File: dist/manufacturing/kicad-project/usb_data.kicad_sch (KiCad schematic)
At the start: 8 parts, among them J10 J10

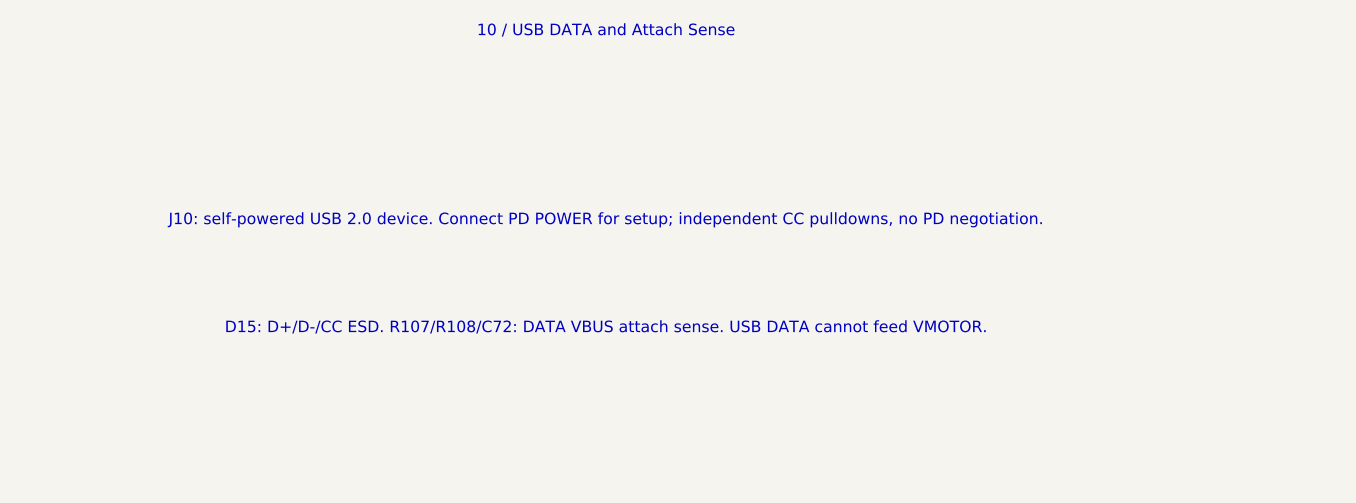
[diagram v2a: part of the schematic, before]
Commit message: Complete top-side routing and verify reference-board ECO
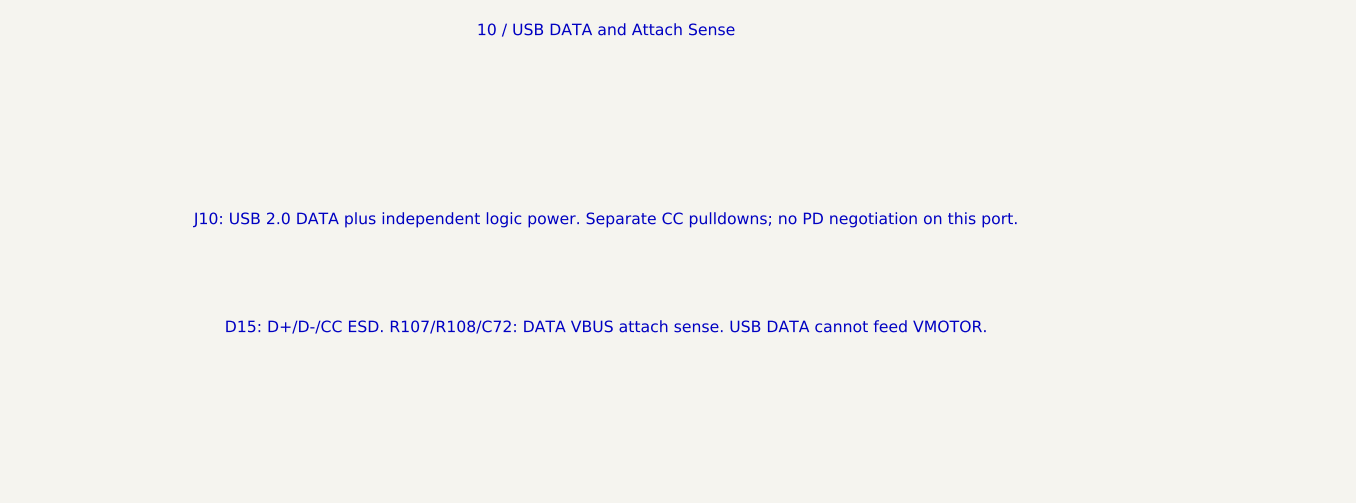
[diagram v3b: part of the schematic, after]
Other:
- note added: "J10: USB 2.0 DATA plus independent logic power. Separate CC pulldowns; no PD negotiation on this port."
- note removed: "J10: self-powered USB 2.0 device. Connect PD POWER for setup; independent CC pulldowns, no PD negotiation."
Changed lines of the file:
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@@
     (instances
       (project ""
-        (path "/4ef2daa1-40fc-426a-abb2-c834ba40a3c9/d0985985-ab5f-41ca-a28b-92bc3b6995fd"
+        (path "/953e0ace-4c89-4879-a4e2-9aa73ffc3208/12d136b2-94e5-4882-b24e-859549138c6a"
           (reference "R107")
           (unit 1)
@@
     (instances
       (project ""
-        (path "/4ef2daa1-40fc-426a-abb2-c834ba40a3c9/d0985985-ab5f-41ca-a28b-92bc3b6995fd"
+        (path "/953e0ace-4c89-4879-a4e2-9aa73ffc3208/12d136b2-94e5-4882-b24e-859549138c6a"
           (reference "R108")
           (unit 1)
@@
     (instances
       (project ""
-        (path "/4ef2daa1-40fc-426a-abb2-c834ba40a3c9/d0985985-ab5f-41ca-a28b-92bc3b6995fd"
+        (path "/953e0ace-4c89-4879-a4e2-9aa73ffc3208/12d136b2-94e5-4882-b24e-859549138c6a"
           (reference "C72")
           (unit 1)
@@
     (instances
       (project ""
-        (path "/4ef2daa1-40fc-426a-abb2-c834ba40a3c9/d0985985-ab5f-41ca-a28b-92bc3b6995fd"
+        (path "/953e0ace-4c89-4879-a4e2-9aa73ffc3208/12d136b2-94e5-4882-b24e-859549138c6a"
           (reference "J10")
           (unit 1)
@@
     (instances
       (project ""
-        (path "/4ef2daa1-40fc-426a-abb2-c834ba40a3c9/d0985985-ab5f-41ca-a28b-92bc3b6995fd"
+        (path "/953e0ace-4c89-4879-a4e2-9aa73ffc3208/12d136b2-94e5-4882-b24e-859549138c6a"
           (reference "R105")
           (unit 1)
@@
     (instances
       (project ""
-        (path "/4ef2daa1-40fc-426a-abb2-c834ba40a3c9/d0985985-ab5f-41ca-a28b-92bc3b6995fd"
+        (path "/953e0ace-4c89-4879-a4e2-9aa73ffc3208/12d136b2-94e5-4882-b24e-859549138c6a"
           (reference "R106")
           (unit 1)
@@
     (instances
       (project ""
-        (path "/4ef2daa1-40fc-426a-abb2-c834ba40a3c9/d0985985-ab5f-41ca-a28b-92bc3b6995fd"
+        (path "/953e0ace-4c89-4879-a4e2-9aa73ffc3208/12d136b2-94e5-4882-b24e-859549138c6a"
           (reference "D15")
           (unit 1)
@@
     (instances
       (project ""
-        (path "/4ef2daa1-40fc-426a-abb2-c834ba40a3c9/d0985985-ab5f-41ca-a28b-92bc3b6995fd"
+        (path "/953e0ace-4c89-4879-a4e2-9aa73ffc3208/12d136b2-94e5-4882-b24e-859549138c6a"
           (reference "C73")
           (unit 1)
@@
     )
   )
-  (text "J10: self-powered USB 2.0 device. Connect PD POWER for setup; independent CC pulldowns, no PD negotiation."
+  (text "J10: USB 2.0 DATA plus independent logic power. Separate CC pulldowns; no PD negotiation on this port."
     (at 26.174999999999997 -65.5 0)
     (effects
